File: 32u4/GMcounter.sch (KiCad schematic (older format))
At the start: 40 parts, among them P1 CONN_01X01, P2 CONN_01X01, P3 CONN_01X01, P4 USB_A, Q1 MMBT3904, Q2 STL128DN, Q3 MMBT3904, Q4 CSTLA_T, U1 TLC555CP, U2 ATmega32U4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

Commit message: updated with proper resonator footprint
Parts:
- Q4: footprint murata-resonators:murata-resonators-CSTLA_T -> MyKiCadLibs:Murata-16mhz-Resonator
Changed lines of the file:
@@
 F 0 "Q4" H 9470 2330 50  0000 L BNN
 F 1 "CSTLA_T" V 9900 1850 50  0000 L BNN
-F 2 "murata-resonators:murata-resonators-CSTLA_T" H 9650 2350 50  0001 C CNN
+F 2 "MyKiCadLibs:Murata-16mhz-Resonator" H 9650 2350 50  0001 C CNN
 F 3 "" H 9650 2200 60  0000 C CNN
 	1    9650 2200

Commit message: updates
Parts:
- added D5: one_diode_please, Diodes_SMD:SOD-323, symbol D
- added P5: CONN_01X03, Pin_Headers:Pin_Header_Straight_1x03, symbol CONN_01X03
- added P6: CONN_02X04, Pin_Headers:Pin_Header_Straight_2x04, symbol CONN_02X04
- P4: footprint USB_oshpark:USB_A_CNCTech_modified_for_oshpark -> USB_oshpark:USB_A_Multicomp_thruhole_oshpark
- R14: value 22 -> 10k
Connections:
- net +3V3: now also P5.1 (P1); no longer L1.2, R4.2, U1.8 (VCC)
- net +5V: now also D5.2 (A), P5.3 (P3), P6.2 (P2); no longer P4.1 (VCC)
- net GND: now also P6.6 (P6)
- net MOSI: now reaches U2.10 ((PDI/MOSI/PCINT2)PB2)
- net MOSI: now also P6.4 (P4)
- net MISO: now reaches U2.11 ((PDO/MISO/PCINT3)PB3)
- net MISO: now also P6.1 (P1)
- net RST: now reaches R14.2, U2.13 (RESET)
- net RST: now also P6.5 (P5)
- net SCL: now reaches U2.18 ((OC0B/SCL/INT0)PD0)
- net SCL: now also P6.7 (P7)
- net SDA: now reaches U2.19 ((SDA/INT1)PD1)
- net SDA: now also P6.8 (P8)
- net SCLK: now reaches U2.9 ((SCLK/PCINT1)PB1)
- net SCLK: now also P6.3 (P3)
- new net: L1.2, P5.2 (P2), R4.2, U1.8 (VCC)
- new net: D5.1 (K), P4.1 (VCC)
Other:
- moved on the sheet: P4

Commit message: updates
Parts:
- added P7: CONN_01X03, Pin_Headers:Pin_Header_Straight_1x03, symbol CONN_01X03
- D5: footprint Diodes_SMD:SOD-323 -> Diodes_SMD:SMA_Standard
- P4: footprint USB_oshpark:USB_A_Multicomp_thruhole_oshpark -> MyKiCadLibs:USB_Micro-B-OshPark
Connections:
- net +3V3: now also P7.1 (P1)
- net +5V: now also P7.3 (P3)
- net GND: now also P7.2 (P2)
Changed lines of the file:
@@
 Connection ~ 2000 6950
 $Comp
-L GND #PWR17
+L GND #PWR20
 U 1 1 5BE1C970
 P 9500 850
-F 0 "#PWR17" H 9500 600 50  0001 C CNN
+F 0 "#PWR20" H 9500 600 50  0001 C CNN
 F 1 "GND" H 9500 700 50  0000 C CNN
 F 2 "" H 9500 850 50  0000 C CNN
@@
 	10300 3350 9800 3350
 $Comp
-L +5V #PWR16
+L +5V #PWR19
 U 1 1 5BE1DE07
 P 9450 4450
-F 0 "#PWR16" H 9450 4300 50  0001 C CNN
+F 0 "#PWR19" H 9450 4300 50  0001 C CNN
 F 1 "+5V" H 9450 4590 50  0000 C CNN
 F 2 "" H 9450 4450 50  0000 C CNN
@@
 F 0 "P4" H 5250 4800 50  0000 C CNN
 F 1 "USB_A" H 5000 5200 50  0000 C CNN
-F 2 "USB_oshpark:USB_A_Multicomp_thruhole_oshpark" V 5000 4900 50  0001 C CNN
+F 2 "MyKiCadLibs:USB_Micro-B-OshPark" V 5000 4900 50  0001 C CNN
 F 3 "" V 5000 4900 50  0000 C CNN
 	1    5050 5000
@@
 D-
 $Comp
-L GND #PWR12
+L GND #PWR15
 U 1 1 5BE1E54E
 P 5450 5450
-F 0 "#PWR12" H 5450 5200 50  0001 C CNN
+F 0 "#PWR15" H 5450 5200 50  0001 C CNN
 F 1 "GND" H 5450 5300 50  0000 C CNN
 F 2 "" H 5450 5450 50  0000 C CNN
@@
 $EndComp
 $Comp
-L GND #PWR18
+L GND #PWR21
 U 1 1 5BE22037
 P 9850 4450
-F 0 "#PWR18" H 9850 4200 50  0001 C CNN
+F 0 "#PWR21" H 9850 4200 50  0001 C CNN
 F 1 "GND" H 9850 4300 50  0000 C CNN
 F 2 "" H 9850 4450 50  0000 C CNN
@@
 $EndComp
 $Comp
-L +5V #PWR19
+L +5V #PWR22
 U 1 1 5BE236F8
 P 10000 2950
-F 0 "#PWR19" H 10000 2800 50  0001 C CNN
+F 0 "#PWR22" H 10000 2800 50  0001 C CNN
 F 1 "+5V" H 10000 3090 50  0000 C CNN
 F 2 "" H 10000 2950 50  0000 C CNN
@@
 	9650 1950 9650 2000
 $Comp
-L GND #PWR20
+L GND #PWR23
 U 1 1 5BE23CE5
 P 10150 1900
-F 0 "#PWR20" H 10150 1650 50  0001 C CNN
+F 0 "#PWR23" H 10150 1650 50  0001 C CNN
 F 1 "GND" H 10150 1750 50  0000 C CNN
 F 2 "" H 10150 1900 50  0000 C CNN
@@
 $EndComp
 $Comp
-L GND #PWR13
+L GND #PWR16
 U 1 1 5BE241C1
 P 5650 1350
-F 0 "#PWR13" H 5650 1100 50  0001 C CNN
+F 0 "#PWR16" H 5650 1100 50  0001 C CNN
 F 1 "GND" H 5650 1200 50  0000 C CNN
 F 2 "" H 5650 1350 50  0000 C CNN
@@
 	10250 3250 10250 3050
 $Comp
-L GND #PWR21
+L GND #PWR24
 U 1 1 5BE251E4
 P 10350 2550
-F 0 "#PWR21" H 10350 2300 50  0001 C CNN
+F 0 "#PWR24" H 10350 2300 50  0001 C CNN
 F 1 "GND" H 10350 2400 50  0000 C CNN
 F 2 "" H 10350 2550 50  0000 C CNN
@@
 F 0 "D5" H 4600 5550 50  0000 C CNN
 F 1 "one_diode_please" H 4800 5250 50  0000 C CNN
-F 2 "Diodes_SMD:SOD-323" H 4600 5450 50  0001 C CNN
+F 2 "Diodes_SMD:SMA_Standard" H 4600 5450 50  0001 C CNN
 F 3 "" H 4600 5450 50  0000 C CNN
 	1    4600 5450
@@
 	8200 5550 8000 5550
 $Comp
-L +5V #PWR14
+L +5V #PWR17
 U 1 1 5BE27409
 P 8100 5350
-F 0 "#PWR14" H 8100 5200 50  0001 C CNN
+F 0 "#PWR17" H 8100 5200 50  0001 C CNN
 F 1 "+5V" H 8100 5490 50  0000 C CNN
 F 2 "" H 8100 5350 50  0000 C CNN
@@
 $EndComp
 $Comp
-L GND #PWR15
+L GND #PWR18
 U 1 1 5BE27495
 P 8550 5650
-F 0 "#PWR15" H 8550 5400 50  0001 C CNN
+F 0 "#PWR18" H 8550 5400 50  0001 C CNN
 F 1 "GND" H 8550 5500 50  0000 C CNN
 F 2 "" H 8550 5650 50  0000 C CNN
@@
 Wire Wire Line
 	6850 2950 6700 2950
+$Comp
+L +3.3V #PWR12
+U 1 1 5BE29C6A
+P 4900 6700
+F 0 "#PWR12" H 4900 6550 50  0001 C CNN
+F 1 "+3.3V" H 4900 6840 50  0000 C CNN
+F 2 "" H 4900 6700 50  0000 C CNN
+F 3 "" H 4900 6700 50  0000 C CNN
+	1    4900 6700
+	0    -1   -1   0
+$EndComp
+$Comp
+L CONN_01X03 P7
+U 1 1 5BE29C70
+P 5100 6400
+F 0 "P7" H 5100 6600 50  0000 C CNN
+F 1 "CONN_01X03" V 5200 6400 50  0000 C CNN
+F 2 "Pin_Headers:Pin_Header_Straight_1x03" H 5100 6400 50  0001 C CNN
+F 3 "" H 5100 6400 50  0000 C CNN
+	1    5100 6400
+	0    -1   -1   0
+$EndComp
+$Comp
+L +5V #PWR14
+U 1 1 5BE29C76
+P 5300 6700
+F 0 "#PWR14" H 5300 6550 50  0001 C CNN
+F 1 "+5V" H 5300 6840 50  0000 C CNN
+F 2 "" H 5300 6700 50  0000 C CNN
+F 3 "" H 5300 6700 50  0000 C CNN
+	1    5300 6700
+	0    1    1    0
+$EndComp
+Wire Wire Line
+	4900 6700 5000 6700
+Wire Wire Line
+	5000 6700 5000 6600
+Wire Wire Line
+	5300 6700 5200 6700
+Wire Wire Line
+	5200 6700 5200 6600
+$Comp
+L GND #PWR13
+U 1 1 5BE29D07
+P 5100 6850
+F 0 "#PWR13" H 5100 6600 50  0001 C CNN
+F 1 "GND" H 5100 6700 50  0000 C CNN
+F 2 "" H 5100 6850 50  0000 C CNN
+F 3 "" H 5100 6850 50  0000 C CNN
+	1    5100 6850
+	1    0    0    -1
+$EndComp
+Wire Wire Line
+	5100 6600 5100 6850
 $EndSCHEMATC

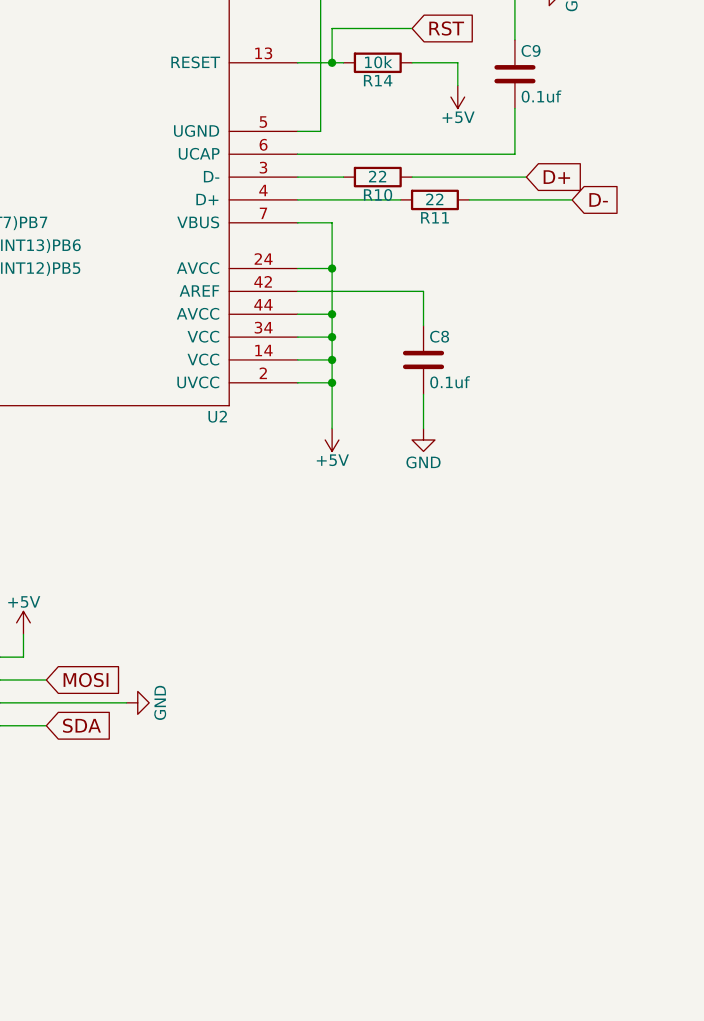
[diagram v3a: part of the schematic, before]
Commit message: changed foot print for inductor, changed design rules
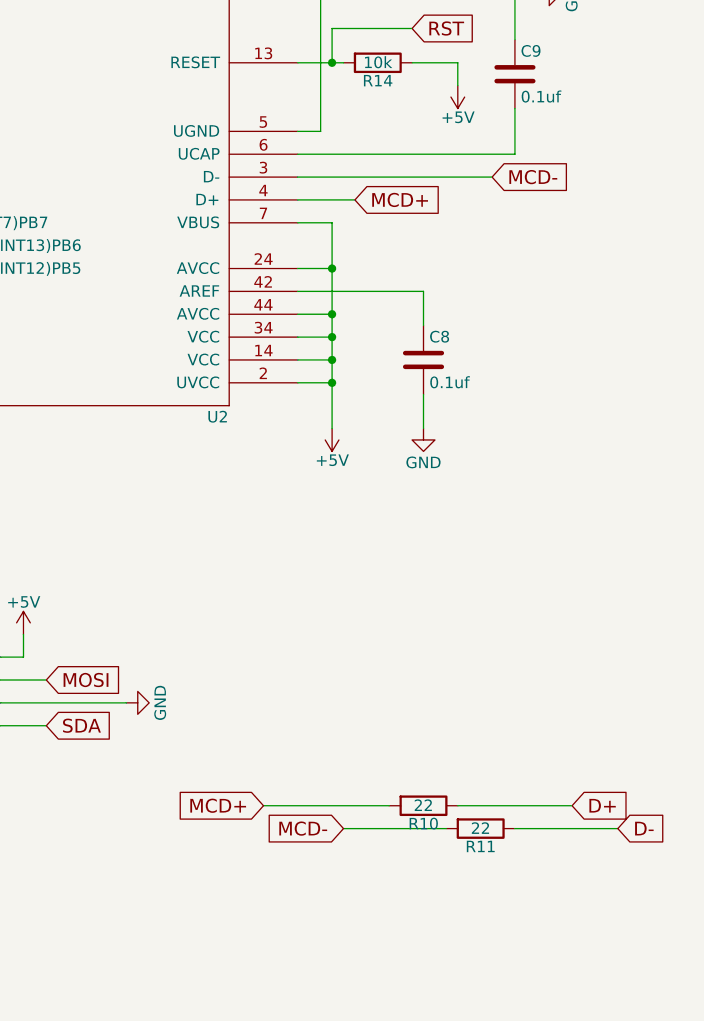
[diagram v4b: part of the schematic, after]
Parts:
- L1: footprint SMD_Packages:SMD-1210_Pol -> Inductors:SELF-WE-PD-XXL
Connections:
- net MCD+: now reaches R10.2
- net MCD+: now also U2.4 (D+); no longer U2.3 (D-)
- net MCD-: now reaches R11.2
- net MCD-: now also U2.3 (D-); no longer U2.4 (D+)
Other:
- moved on the sheet: R10, R11
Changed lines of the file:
@@
 $EndComp
 $Comp
-L GND #PWR4
+L GND #PWR01
 U 1 1 5BE0E4DE
 P 2500 4100
-F 0 "#PWR4" H 2500 3850 50  0001 C CNN
+F 0 "#PWR01" H 2500 3850 50  0001 C CNN
 F 1 "GND" H 2500 3950 50  0000 C CNN
 F 2 "" H 2500 4100 50  0000 C CNN
@@
 F 0 "L1" H 3750 1950 50  0000 L CNN
 F 1 "10mH" H 3550 1850 50  0000 L CNN
-F 2 "SMD_Packages:SMD-1210_Pol" H 3900 1900 50  0001 C CNN
+F 2 "Inductors:SELF-WE-PD-XXL" H 3900 1900 50  0001 C CNN
 F 3 "" H 3900 1900 50  0000 C CNN
 	1    3900 1900
@@
 $EndComp
 $Comp
-L GND #PWR11
+L GND #PWR02
 U 1 1 5BE0EE6A
 P 4750 2900
-F 0 "#PWR11" H 4750 2650 50  0001 C CNN
+F 0 "#PWR02" H 4750 2650 50  0001 C CNN
 F 1 "GND" H 4750 2750 50  0000 C CNN
 F 2 "" H 4750 2900 50  0000 C CNN
@@
 	3500 3150 3500 2150
 $Comp
-L +3.3V #PWR6
+L +3.3V #PWR03
 U 1 1 5BE0F465
 P 3300 1200
-F 0 "#PWR6" H 3300 1050 50  0001 C CNN
+F 0 "#PWR03" H 3300 1050 50  0001 C CNN
 F 1 "+3.3V" H 3300 1340 50  0000 C CNN
 F 2 "" H 3300 1200 50  0000 C CNN
@@
 Connection ~ 3900 3350
 $Comp
-L GND #PWR7
+L GND #PWR04
 U 1 1 5BE0F743
 P 3500 4800
-F 0 "#PWR7" H 3500 4550 50  0001 C CNN
+F 0 "#PWR04" H 3500 4550 50  0001 C CNN
 F 1 "GND" H 3500 4650 50  0000 C CNN
 F 2 "" H 3500 4800 50  0000 C CNN
@@
 $EndComp
 $Comp
-L GND #PWR1
+L GND #PWR05
 U 1 1 5BE10009
 P 1600 6250
-F 0 "#PWR1" H 1600 6000 50  0001 C CNN
+F 0 "#PWR05" H 1600 6000 50  0001 C CNN
 F 1 "GND" H 1600 6100 50  0000 C CNN
 F 2 "" H 1600 6250 50  0000 C CNN
@@
 $EndComp
 $Comp
-L +3.3V #PWR3
+L +3.3V #PWR06
 U 1 1 5BE102E8
 P 2250 4750
-F 0 "#PWR3" H 2250 4600 50  0001 C CNN
+F 0 "#PWR06" H 2250 4600 50  0001 C CNN
 F 1 "+3.3V" H 2250 4890 50  0000 C CNN
 F 2 "" H 2250 4750 50  0000 C CNN
@@
 $EndComp
 $Comp
-L +5V #PWR8
+L +5V #PWR07
 U 1 1 5BE1C0A2
 P 3550 7450
-F 0 "#PWR8" H 3550 7300 50  0001 C CNN
+F 0 "#PWR07" H 3550 7300 50  0001 C CNN
 F 1 "+5V" H 3550 7590 50  0000 C CNN
 F 2 "" H 3550 7450 50  0000 C CNN
@@
 $EndComp
 $Comp
-L GND #PWR5
+L GND #PWR08
 U 1 1 5BE1C105
 P 2500 6500
-F 0 "#PWR5" H 2500 6250 50  0001 C CNN
+F 0 "#PWR08" H 2500 6250 50  0001 C CNN
 F 1 "GND" H 2500 6350 50  0000 C CNN
 F 2 "" H 2500 6500 50  0000 C CNN
@@
 	3550 7450 2800 7450
 $Comp
-L +3.3V #PWR2
+L +3.3V #PWR09
 U 1 1 5BE1C29E
 P 1600 7450
-F 0 "#PWR2" H 1600 7300 50  0001 C CNN
+F 0 "#PWR09" H 1600 7300 50  0001 C CNN
 F 1 "+3.3V" H 1600 7590 50  0000 C CNN
 F 2 "" H 1600 7450 50  0000 C CNN
@@
 Connection ~ 2000 6950
 $Comp
-L GND #PWR20
+L GND #PWR010
 U 1 1 5BE1C970
 P 9500 850
-F 0 "#PWR20" H 9500 600 50  0001 C CNN
+F 0 "#PWR010" H 9500 600 50  0001 C CNN
 F 1 "GND" H 9500 700 50  0000 C CNN
 F 2 "" H 9500 850 50  0000 C CNN
@@
 L R R10
 U 1 1 5BE1D4C8
-P 9650 3350
-F 0 "R10" V 9730 3350 50  0000 C CNN
-F 1 "22" V 9650 3350 50  0000 C CNN
-F 2 "Resistors_SMD:R_1206" V 9580 3350 50  0001 C CNN
-F 3 "" H 9650 3350 50  0000 C CNN
-	1    9650 3350
+P 9850 6100
+F 0 "R10" V 9930 6100 50  0000 C CNN
+F 1 "22" V 9850 6100 50  0000 C CNN
+F 2 "Resistors_SMD:R_1206" V 9780 6100 50  0001 C CNN
+F 3 "" H 9850 6100 50  0000 C CNN
+	1    9850 6100
 	0    1    1    0
 $EndComp
@@
 L R R11
 U 1 1 5BE1D5A6
-P 9900 3450
-F 0 "R11" V 9980 3450 50  0000 C CNN
-F 1 "22" V 9900 3450 50  0000 C CNN
-F 2 "Resistors_SMD:R_1206" V 9830 3450 50  0001 C CNN
-F 3 "" H 9900 3450 50  0000 C CNN
-	1    9900 3450
+P 10100 6200
+F 0 "R11" V 10180 6200 50  0000 C CNN
+F 1 "22" V 10100 6200 50  0000 C CNN
+F 2 "Resistors_SMD:R_1206" V 10030 6200 50  0001 C CNN
+F 3 "" H 10100 6200 50  0000 C CNN
+	1    10100 6200
 	0    1    1    0
 $EndComp
 Wire Wire Line
-	9500 3350 9300 3350
-Wire Wire Line
-	9750 3450 9300 3450
-Text GLabel 10300 3350 2    60   Input ~ 0
+	9950 6200 9500 6200
+Text GLabel 10500 6100 2    60   Input ~ 0
 D+
-Text GLabel 10500 3450 2    60   Input ~ 0
+Text GLabel 10700 6200 2    60   Input ~ 0
 D-
 Wire Wire Line
-	10500 3450 10050 3450
-Wire Wire Line
-	10300 3350 9800 3350
-$Comp
-L +5V #PWR19
+	10700 6200 10250 6200
+Wire Wire Line
+	10500 6100 10000 6100
+$Comp
+L +5V #PWR011
 U 1 1 5BE1DE07
 P 9450 4450
-F 0 "#PWR19" H 9450 4300 50  0001 C CNN
+F 0 "#PWR011" H 9450 4300 50  0001 C CNN
 F 1 "+5V" H 9450 4590 50  0000 C CNN
 F 2 "" H 9450 4450 50  0000 C CNN
@@
 $EndComp
 $Comp
-L +5V #PWR10
+L +5V #PWR012
 U 1 1 5BE1E1BC
 P 4400 5450
-F 0 "#PWR10" H 4400 5300 50  0001 C CNN
+F 0 "#PWR012" H 4400 5300 50  0001 C CNN
 F 1 "+5V" H 4400 5590 50  0000 C CNN
 F 2 "" H 4400 5450 50  0000 C CNN
@@
 D-
 $Comp
-L GND #PWR15
+L GND #PWR013
 U 1 1 5BE1E54E
 P 5450 5450
-F 0 "#PWR15" H 5450 5200 50  0001 C CNN
+F 0 "#PWR013" H 5450 5200 50  0001 C CNN
 F 1 "GND" H 5450 5300 50  0000 C CNN
 F 2 "" H 5450 5450 50  0000 C CNN
@@
 $EndComp
 $Comp
-L GND #PWR21
+L GND #PWR014
 U 1 1 5BE22037
 P 9850 4450
-F 0 "#PWR21" H 9850 4200 50  0001 C CNN
+F 0 "#PWR014" H 9850 4200 50  0001 C CNN
 F 1 "GND" H 9850 4300 50  0000 C CNN
 F 2 "" H 9850 4450 50  0000 C CNN
@@
 $EndComp
 $Comp
-L +5V #PWR22
+L +5V #PWR015
 U 1 1 5BE236F8
 P 10000 2950
-F 0 "#PWR22" H 10000 2800 50  0001 C CNN
+F 0 "#PWR015" H 10000 2800 50  0001 C CNN
 F 1 "+5V" H 10000 3090 50  0000 C CNN
 F 2 "" H 10000 2950 50  0000 C CNN
@@
 	9650 1950 9650 2000
 $Comp
-L GND #PWR23
+L GND #PWR016
 U 1 1 5BE23CE5
 P 10150 1900
-F 0 "#PWR23" H 10150 1650 50  0001 C CNN
+F 0 "#PWR016" H 10150 1650 50  0001 C CNN
 F 1 "GND" H 10150 1750 50  0000 C CNN
 F 2 "" H 10150 1900 50  0000 C CNN
@@
 $EndComp
 $Comp
-L GND #PWR16
+L GND #PWR017
 U 1 1 5BE241C1
 P 5650 1350
-F 0 "#PWR16" H 5650 1100 50  0001 C CNN
+F 0 "#PWR017" H 5650 1100 50  0001 C CNN
 F 1 "GND" H 5650 1200 50  0000 C CNN
 F 2 "" H 5650 1350 50  0000 C CNN
@@
 	10250 3250 10250 3050
 $Comp
-L GND #PWR24
+L GND #PWR018
 U 1 1 5BE251E4
 P 10350 2550
-F 0 "#PWR24" H 10350 2300 50  0001 C CNN
+F 0 "#PWR018" H 10350 2300 50  0001 C CNN
 F 1 "GND" H 10350 2400 50  0000 C CNN
 F 2 "" H 10350 2550 50  0000 C CNN
@@
 $EndComp
 $Comp
-L +5V #PWR9
+L +5V #PWR019
 U 1 1 5BE263F9
 P 3700 1200
-F 0 "#PWR9" H 3700 1050 50  0001 C CNN
+F 0 "#PWR019" H 3700 1050 50  0001 C CNN
 F 1 "+5V" H 3700 1340 50  0000 C CNN
 F 2 "" H 3700 1200 50  0000 C CNN
@@
 	8200 5550 8000 5550
 $Comp
-L +5V #PWR17
+L +5V #PWR020
 U 1 1 5BE27409
 P 8100 5350
-F 0 "#PWR17" H 8100 5200 50  0001 C CNN
+F 0 "#PWR020" H 8100 5200 50  0001 C CNN
 F 1 "+5V" H 8100 5490 50  0000 C CNN
 F 2 "" H 8100 5350 50  0000 C CNN
@@
 $EndComp
 $Comp
-L GND #PWR18
+L GND #PWR021
 U 1 1 5BE27495
 P 8550 5650
-F 0 "#PWR18" H 8550 5400 50  0001 C CNN
+F 0 "#PWR021" H 8550 5400 50  0001 C CNN
 F 1 "GND" H 8550 5500 50  0000 C CNN
 F 2 "" H 8550 5650 50  0000 C CNN
@@
 	6850 2950 6700 2950
 $Comp
-L +3.3V #PWR12
+L +3.3V #PWR022
 U 1 1 5BE29C6A
 P 4900 6700
-F 0 "#PWR12" H 4900 6550 50  0001 C CNN
+F 0 "#PWR022" H 4900 6550 50  0001 C CNN
 F 1 "+3.3V" H 4900 6840 50  0000 C CNN
 F 2 "" H 4900 6700 50  0000 C CNN
@@
 $EndComp
 $Comp
-L +5V #PWR14
+L +5V #PWR023
 U 1 1 5BE29C76
 P 5300 6700
-F 0 "#PWR14" H 5300 6550 50  0001 C CNN
+F 0 "#PWR023" H 5300 6550 50  0001 C CNN
 F 1 "+5V" H 5300 6840 50  0000 C CNN
 F 2 "" H 5300 6700 50  0000 C CNN
@@
 	5200 6700 5200 6600
 $Comp
-L GND #PWR13
+L GND #PWR024
 U 1 1 5BE29D07
 P 5100 6850
-F 0 "#PWR13" H 5100 6600 50  0001 C CNN
+F 0 "#PWR024" H 5100 6600 50  0001 C CNN
 F 1 "GND" H 5100 6700 50  0000 C CNN
 F 2 "" H 5100 6850 50  0000 C CNN
@@
 Wire Wire Line
 	5100 6600 5100 6850
+Text GLabel 9150 6100 0    60   Input ~ 0
+MCD+
+Text GLabel 9500 6200 0    60   Input ~ 0
+MCD-
+Wire Wire Line
+	9150 6100 9700 6100
+Text GLabel 9550 3450 2    60   Input ~ 0
+MCD+
+Text GLabel 10150 3350 2    60   Input ~ 0
+MCD-
+Wire Wire Line
+	10150 3350 9300 3350
+Wire Wire Line
+	9550 3450 9300 3450
 $EndSCHEMATC

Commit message: updated to kicad 5
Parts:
- removed P6: CONN_02X04, Pin_Headers:Pin_Header_Straight_2x04, symbol CONN_02X04
- added J1: Conn_02x05_Counter_Clockwise, Connector_PinHeader_2.54mm:PinHeader_2x05_P2.54mm_Vertical, symbol Connector_Generic:Conn_02x05_Counter_Clockwise
- C1, C2, C3, C4, C6: footprint Capacitors_Tantalum_SMD:TantalC_SizeA_EIA-3216_Reflow -> Capacitor_Tantalum_SMD:CP_EIA-3216-12_Kemet-S; symbol CP -> GMcounter-rescue:CP
- C5, C7, C8, C9: footprint Capacitors_SMD:C_1206 -> Capacitor_SMD:C_1206_3216Metric; symbol C -> GMcounter-rescue:C
- D1: footprint Diodes_SMD:SOD-323 -> Diode_SMD:D_SOD-323; symbol D -> GMcounter-rescue:D
- D2: footprint Diodes_SMD:SMC_Standard -> Diode_SMD:D_SMC; symbol D -> GMcounter-rescue:D
- D3, D4: footprint LEDs:LED_0805 -> Diode_SMD:D_0805_2012Metric; symbol LED -> GMcounter-rescue:LED
- D5: footprint Diodes_SMD:SMA_Standard -> Diode_SMD:D_SMA; symbol D -> GMcounter-rescue:D
- L1: symbol L_Small -> GMcounter-rescue:L_Small
- P1, P2, P3: footprint Pin_Headers:Pin_Header_Straight_1x01 -> Connector_PinHeader_2.54mm:PinHeader_1x01_P2.54mm_Vertical; symbol CONN_01X01 -> GMcounter-rescue:CONN_01X01
- P4: symbol USB_A -> GMcounter-rescue:USB_A
- P5, P7: footprint Pin_Headers:Pin_Header_Straight_1x03 -> Connector_PinHeader_2.54mm:PinHeader_1x03_P2.54mm_Vertical; symbol CONN_01X03 -> GMcounter-rescue:CONN_01X03
- Q1, Q3: footprint TO_SOT_Packages_SMD:SOT-23 -> Package_TO_SOT_SMD:SOT-23; symbol MMBT3904 -> GMcounter-rescue:MMBT3904
- Q2: footprint TO_SOT_Packages_SMD:TO-252-2Lead -> Package_TO_SOT_SMD:TO-252-2; symbol BD249C -> GMcounter-rescue:BD249C
- Q4: symbol CSTLA_T -> GMcounter-rescue:CSTLA_T
- R1, R10, R11, R12, R13, R14, R2, R3, R4, R5, R6, R7, R8, R9: footprint Resistors_SMD:R_1206 -> Resistor_SMD:R_1206_3216Metric; symbol R -> GMcounter-rescue:R
- RV1: footprint Potentiometers:Potentiometer_WirePads_Small -> Potentiometer_THT:Potentiometer_Bourns_3296W_Vertical; symbol POT -> GMcounter-rescue:POT
- U1: footprint Housings_SOIC:SOIC-8_3.9x4.9mm_Pitch1.27mm -> Package_SO:SOIC-8_3.9x4.9mm_P1.27mm; symbol TLC555CP -> GMcounter-rescue:TLC555CP
- U2: footprint Housings_QFP:TQFP-44_10x10mm_Pitch0.8mm -> Package_QFP:TQFP-44_10x10mm_P0.8mm; symbol ATmega32U4 -> GMcounter-rescue:ATmega32U4
- U3: footprint TO_SOT_Packages_SMD:SOT-223 -> Package_TO_SOT_SMD:SOT-223; symbol AP1117D33 -> GMcounter-rescue:AP1117D33
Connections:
- net +5V: now also J1.10 (Pin_10)
- net GND: now also J1.8 (Pin_8)
- net MISO: now also J1.1 (Pin_1)
- net MOSI: now also J1.9 (Pin_9)
- net RST: now also J1.3 (Pin_3)
- net SCL: now also J1.4 (Pin_4)
- net SCLK: now also J1.2 (Pin_2)
- net SDA: now also J1.7 (Pin_7)
- net ADC1: now reaches U2.40 ((ADC1)PF1)
- net ADC1: now also J1.5 (Pin_5)
- net ADC0: now reaches U2.41 ((ADC0)PF0)
- net ADC0: now also J1.6 (Pin_6)
